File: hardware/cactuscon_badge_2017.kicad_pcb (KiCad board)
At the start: 2 copper layers, 88.9 x 94.6 mm, 18 parts, among them J1 CONN_01X01, J10 CONN_01X10, J11 CONN_01X10, J12 CONN_01X01, J2 CONN_01X10, J3 CONN_01X10, J4 CONN_01X10, J5 CONN_01X04, J6 CONN_01X10, J7 CONN_01X10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

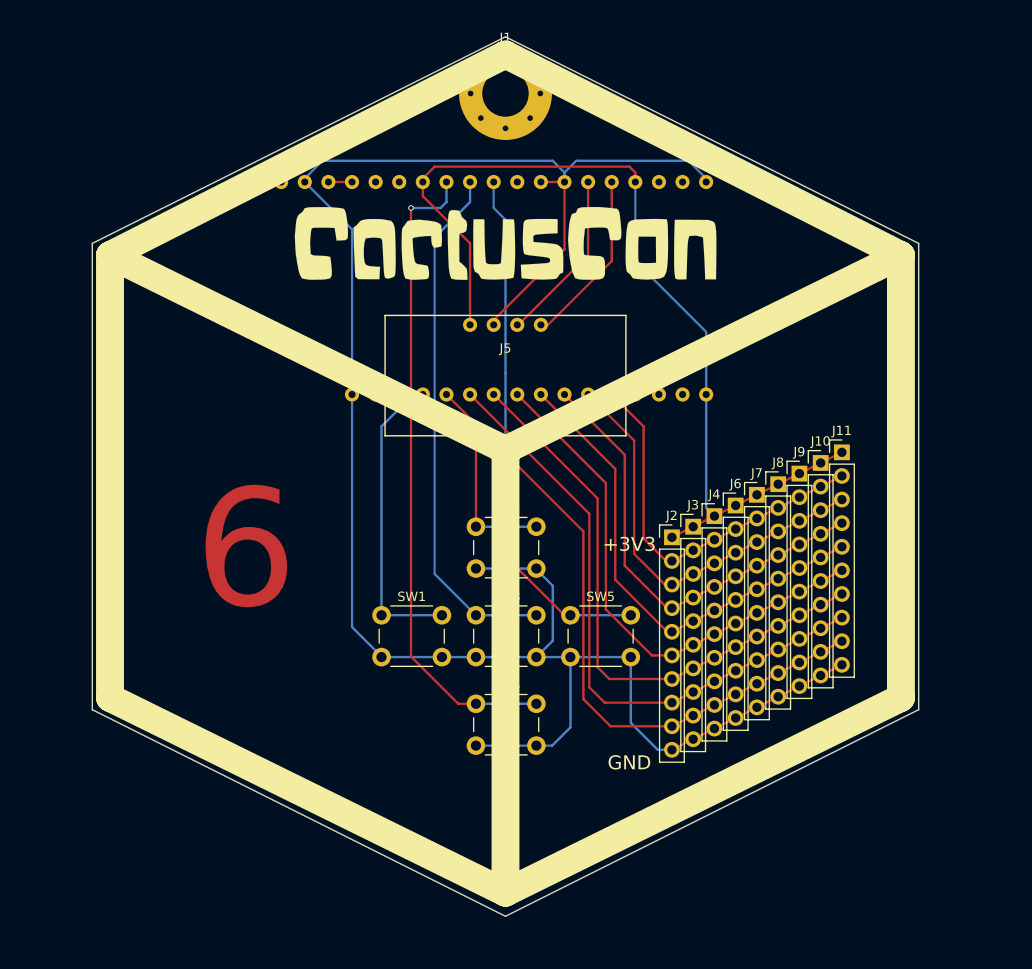
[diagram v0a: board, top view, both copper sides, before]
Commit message: Update art, layout, i2c pins, and fix stray trace
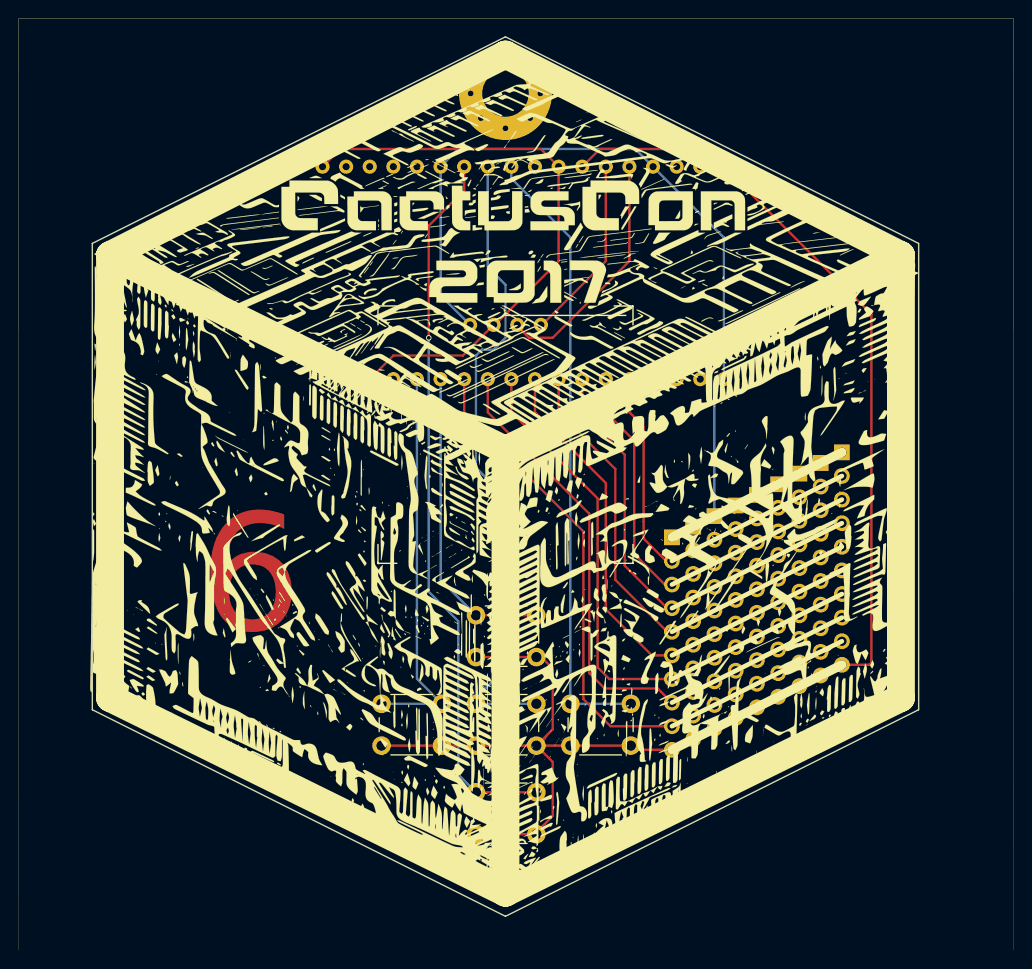
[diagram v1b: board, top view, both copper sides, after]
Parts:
- J10, J11, J2, J3, J4, J6, J7, J8, J9: footprint Pin_Headers:Pin_Header_Straight_1x10_Pitch2.54mm -> CactusCon:10Pin_NoSilk
- J12: footprint CactusCon:CactusCon_Logo -> CactusCon:CactusCon_Full_Badge
- moved J12 25.9 mm to (145.9, 95.8)
- moved SW2 9.53 mm to (141.6, 109.9)
- moved SW4 9.53 mm to (141.6, 128.9)
- moved SW1 9.52 mm to (131.4, 119.4)
- moved SW3 9.52 mm to (141.6, 119.4)
- moved SW5 9.52 mm to (151.8, 119.4)
- moved M1 2.52 mm to (175.9, 73.0)
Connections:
- J5 pad 3: SDA -> SCL
- J5 pad 4: SCL -> SDA
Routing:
- net GND: track 219.2 -> 232.9 mm
- net SEL: track 56.5 -> 68.7 mm
- net LT: track 31.0 -> 42.5 mm
- net UP: track 23.1 -> 33.5 mm
- net RT: track 56.9 -> 66.9 mm, vias 1 -> 0
- net SCL: track 19.0 -> 26.4 mm
- net DN: track 70.1 -> 77.5 mm
- net (no net): track 2.92 -> 0.00 mm
- net Net-(J10-Pad1): track 102.6 -> 104.5 mm
- net SDA: track 18.6 -> 20.0 mm
- net ROW9: track 70.0 -> 70.9 mm
- net ROW7: track 62.9 -> 63.8 mm
- net ROW6: track 57.1 -> 57.9 mm
- net ROW4: track 48.9 -> 49.8 mm
- net ROW3: track 45.1 -> 45.9 mm
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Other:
- board text added: "12"
- board text added: "13"
- board text added: "14"
- board text added: "18"
- board text added: "23"
- board text added: "25"
- board text added: "26"
- board text added: "27"
- board text added: "32"
- board text added: "33"
- board text added: "34"
- board text added: "35"
- board text added: "5"

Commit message: Add repo, partner logos, proto traces to back
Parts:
- added J13: Partners, CactusCon:Partner_Logos, B.Cu at (124.0, 101.5)
- added J14: OSHW, Symbols:OSHW-Logo2_9.8x8mm_SilkScreen, B.Cu at (168.1, 74.5)
- J12: value CONN_01X01 -> Graphic
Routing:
- net GND: track 232.9 -> 295.0 mm
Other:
- board text added: "CC-BY"
- board text added: "github.com/thatch/cactuscon-badge-2017"

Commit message: Add OLED warning/pinout
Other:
- board text added: "OLED other side!"
- board text added: "SDA"
- board text added: "VCC"
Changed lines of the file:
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@@
     (area 100.254999 47.549999 189.305001 142.315001)
     (thickness 1.6)
-    (drawings 45)
+    (drawings 48)
     (tracks 213)
     (zones 0)
@@
       (xy -0.017575 3.712307) (xy 0 3.712308) (xy 0.139878 3.712224)) (layer B.SilkS) (width 0.01))
   )
+  (gr_text SDA (at 152.4 78.74) (layer B.SilkS)
+    (effects (font (size 1.5 1.5) (thickness 0.3)) (justify mirror))
+  )
+  (gr_text VCC (at 137.16 78.74) (layer B.SilkS)
+    (effects (font (size 1.5 1.5) (thickness 0.3)) (justify mirror))
+  )
+  (gr_text "OLED other side!" (at 144.78 74.93) (layer B.SilkS)
+    (effects (font (size 1.5 1.5) (thickness 0.3)) (justify mirror))
+  )
   (gr_text CC-BY (at 168.148 80.137) (layer B.SilkS)

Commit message: Enlarge module holes, note IO side, update renders
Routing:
- net ROW7: track 63.8 -> 61.4 mm
- net ROW8: track 66.8 -> 64.7 mm
- net ROW9: track 70.9 -> 70.1 mm
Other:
- board text added: "<- IO"
